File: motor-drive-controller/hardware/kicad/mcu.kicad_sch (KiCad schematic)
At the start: 23 parts, among them J2 Conn_01x03_Pin, J3 JTAG, J4 J_HALL, SW1 SW_Push, U1 STM32F405RGT6, U2 CR2032, Y1 AAH-181-8.000MHZ

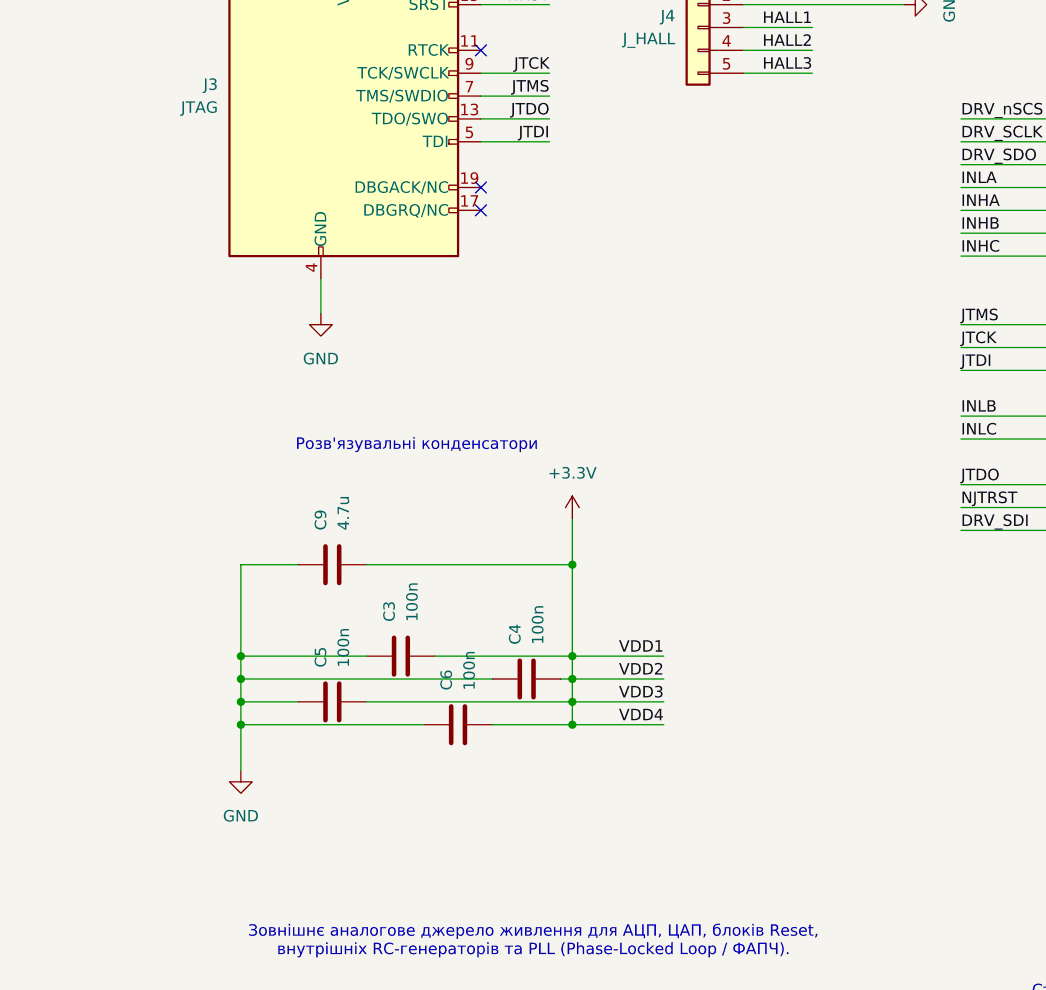
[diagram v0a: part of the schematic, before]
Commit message: feat(motor-drive): add Pull-up resistor to DRV_SDO SPI1
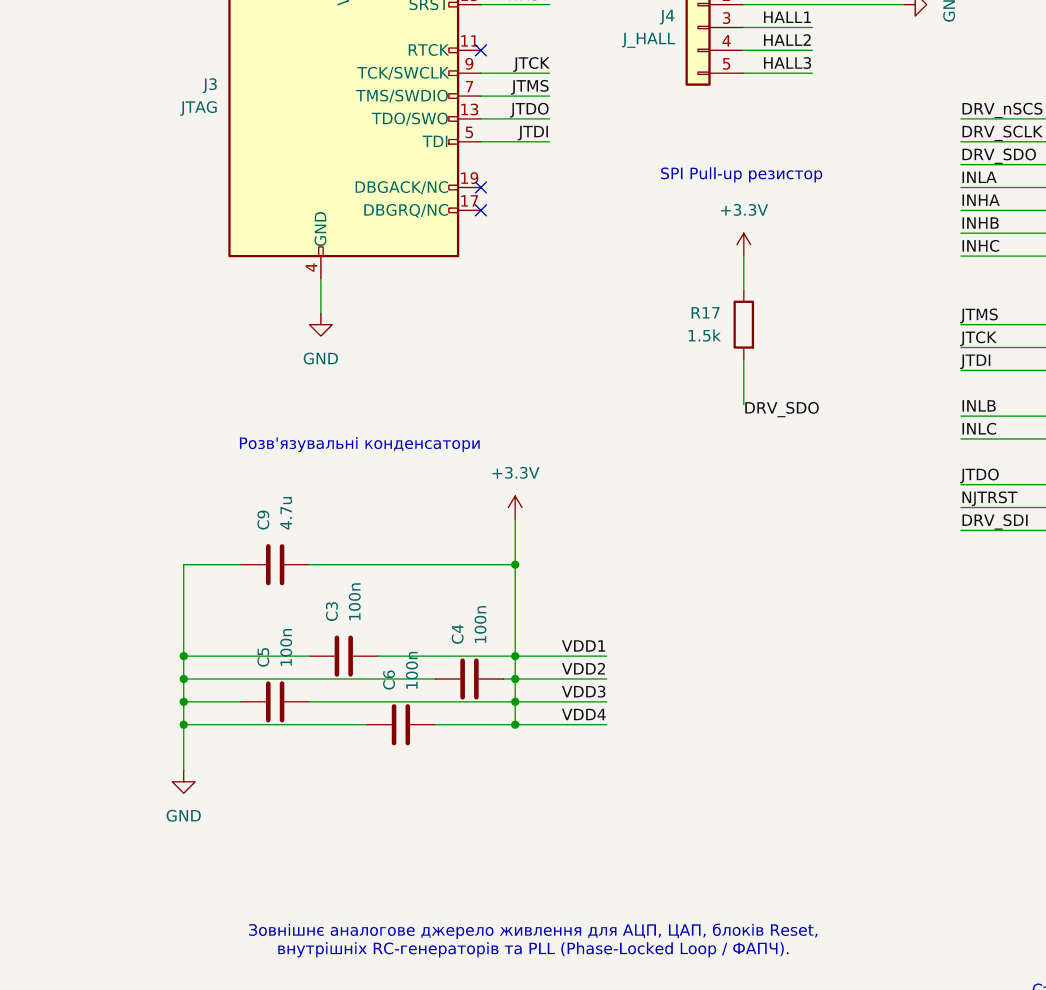
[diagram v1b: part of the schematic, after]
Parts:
- added R17: 1.5k, symbol Device:R
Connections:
- net +3.3V: now also R17.1
- net DRV_SDO: now also R17.2
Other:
- note added: "SPI Pull-up резистор"
- moved on the sheet: C3, C4, C5, C6, C9

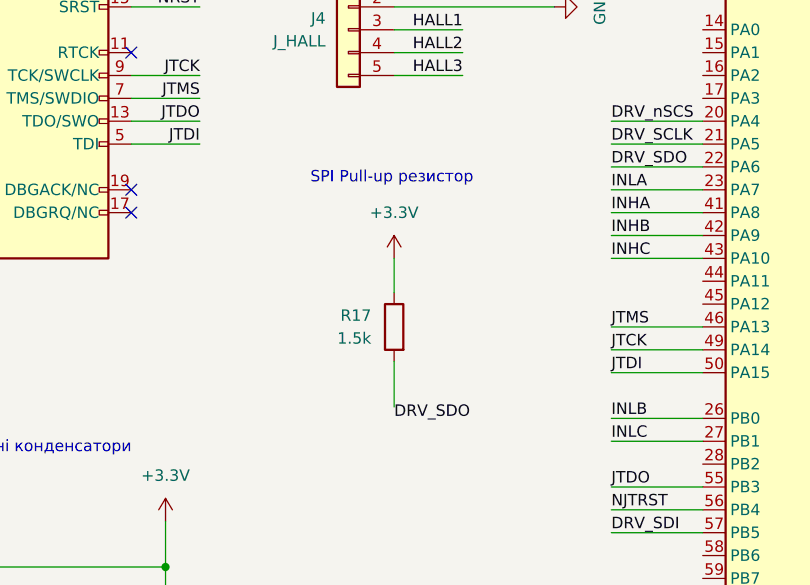
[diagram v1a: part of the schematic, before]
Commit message: feat(motor-drive): add Pull-up resistor to DRV_nSCS SPI1
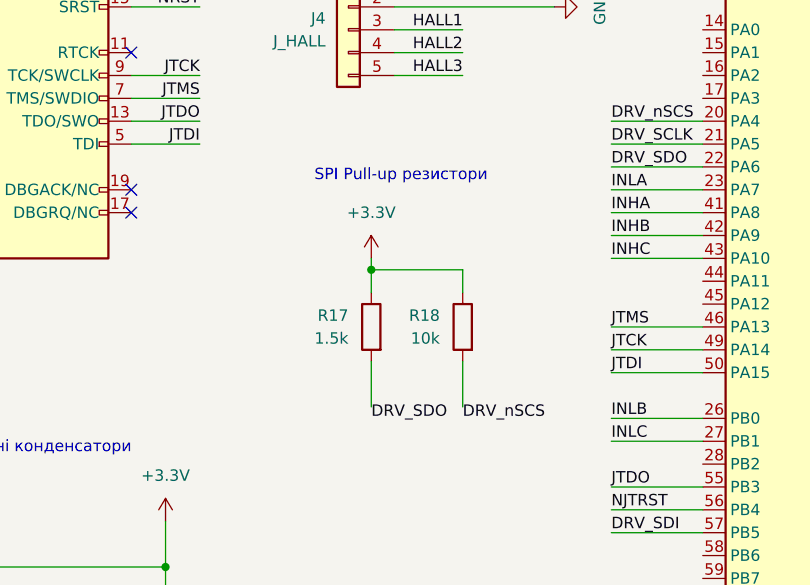
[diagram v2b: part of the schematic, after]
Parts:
- added R18: 10k, symbol Device:R
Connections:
- net +3.3V: now also R18.1
- net DRV_nSCS: now also R18.2
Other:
- note added: "SPI Pull-up резистори"
- note removed: "SPI Pull-up резистор"
- moved on the sheet: R17
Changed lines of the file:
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@@
 		)
 	)
-	(text "SPI Pull-up резистор"
+	(text "SPI Pull-up резистори"
 		(exclude_from_sim no)
-		(at 88.646 64.77 0)
+		(at 89.662 64.516 0)
 		(effects
 			(font
@@
 	)
 	(junction
+		(at 86.36 74.93)
+		(diameter 0)
+		(color 0 0 0 0)
+	)
+	(junction
 		(at 246.38 39.37)
 		(diameter 0)
@@
 	(wire
 		(pts
+			(xy 96.52 74.93) (xy 86.36 74.93)
+		)
+		(stroke
+			(width 0)
+			(type default)
+		)
+	)
+	(wire
+		(pts
 			(xy 238.76 44.45) (xy 240.03 44.45)
 		)
@@
 	(wire
 		(pts
+			(xy 86.36 74.93) (xy 86.36 77.47)
+		)
+		(stroke
+			(width 0)
+			(type default)
+		)
+	)
+	(wire
+		(pts
 			(xy 73.66 123.19) (xy 63.5 123.19)
 		)
@@
 	(wire
 		(pts
-			(xy 88.9 73.66) (xy 88.9 77.47)
+			(xy 86.36 73.66) (xy 86.36 74.93)
 		)
 		(stroke
@@
 	(wire
 		(pts
-			(xy 88.9 90.17) (xy 88.9 85.09)
+			(xy 86.36 90.17) (xy 86.36 85.09)
 		)
 		(stroke
@@
 	(wire
 		(pts
+			(xy 96.52 74.93) (xy 96.52 77.47)
+		)
+		(stroke
+			(width 0)
+			(type default)
+		)
+	)
+	(wire
+		(pts
+			(xy 96.52 85.09) (xy 96.52 90.17)
+		)
+		(stroke
+			(width 0)
+			(type default)
+		)
+	)
+	(wire
+		(pts
 			(xy 95.25 35.56) (xy 95.25 39.37)
 		)
@@
 	)
 	(label "DRV_SDO"
-		(at 88.9 90.17 0)
+		(at 86.36 90.17 0)
+		(effects
+			(font
+				(size 1.27 1.27)
+			)
+			(justify top)
+		)
+	)
+	(label "DRV_nSCS"
+		(at 96.52 90.17 0)
 		(effects
 			(font
@@
 	(symbol
 		(lib_id "power:+3.3V")
-		(at 88.9 73.66 0)
+		(at 86.36 73.66 0)
 		(unit 1)
 		(body_style 1)
@@
 		(fields_autoplaced yes)
 		(property "Reference" "#PWR040"
-			(at 88.9 77.47 0)
+			(at 86.36 77.47 0)
 			(hide yes)
 			(show_name no)
@@
 		)
 		(property "Value" "+3.3V"
-			(at 88.9 68.58 0)
+			(at 86.36 68.58 0)
 			(show_name no)
 			(do_not_autoplace no)
@@
 		)
 		(property "Footprint" ""
-			(at 88.9 73.66 0)
+			(at 86.36 73.66 0)
 			(hide yes)
 			(show_name no)
@@
 		)
 		(property "Datasheet" ""
-			(at 88.9 73.66 0)
+			(at 86.36 73.66 0)
 			(hide yes)
 			(show_name no)
@@
 		)
 		(property "Description" "Power symbol creates a global label with name \"+3.3V\""
-			(at 88.9 73.66 0)
+			(at 86.36 73.66 0)
 			(hide yes)
 			(show_name no)
@@
 	)
 	(symbol
+		(lib_id "Device:R")
+		(at 96.52 81.28 0)
+		(mirror y)
+		(unit 1)
+		(body_style 1)
+		(exclude_from_sim no)
+		(in_bom yes)
+		(on_board yes)
+		(in_pos_files yes)
+		(dnp no)
+		(fields_autoplaced yes)
+		(property "Reference" "R18"
+			(at 93.98 80.0099 0)
+			(show_name no)
+			(do_not_autoplace no)
+			(effects
+				(font
+					(size 1.27 1.27)
+				)
+				(justify left)
+			)
+		)
+		(property "Value" "10k"
+			(at 93.98 82.5499 0)
+			(show_name no)
+			(do_not_autoplace no)
+			(effects
+				(font
+					(size 1.27 1.27)
+				)
+				(justify left)
+			)
+		)
+		(property "Footprint" ""
+			(at 98.298 81.28 90)
+			(hide yes)
+			(show_name no)
+			(do_not_autoplace no)
+			(effects
+				(font
+					(size 1.27 1.27)
+				)
+			)
+		)
+		(property "Datasheet" ""
+			(at 96.52 81.28 0)
+			(hide yes)
+			(show_name no)
+			(do_not_autoplace no)
+			(effects
+				(font
+					(size 1.27 1.27)
+				)
+			)
+		)
+		(property "Description" "Resistor"
+			(at 96.52 81.28 0)
+			(hide yes)
+			(show_name no)
+			(do_not_autoplace no)
+			(effects
+				(font
+					(size 1.27 1.27)
+				)
+			)
+		)
+		(pin "1"
+		)
+		(pin "2"
+		)
+		(instances
+			(project "motor-drive-controller"
+				(path "/b8e0307a-d356-4cd3-91c6-dd251b6e910b/194c8782-4fa9-42ae-9e6d-f27cf422e161"
+					(reference "R18")
+					(unit 1)
+				)
+			)
+		)
+	)
+	(symbol
 		(lib_id "power:+5V")
 		(at 95.25 35.56 0)
@@
 	(symbol
 		(lib_id "Device:R")
-		(at 88.9 81.28 0)
+		(at 86.36 81.28 0)
 		(mirror y)
 		(unit 1)
@@
 		(fields_autoplaced yes)
 		(property "Reference" "R17"
-			(at 86.36 80.0099 0)
+			(at 83.82 80.0099 0)
 			(show_name no)
 			(do_not_autoplace no)
@@
 		)
 		(property "Value" "1.5k"
-			(at 86.36 82.5499 0)
+			(at 83.82 82.5499 0)
 			(show_name no)
 			(do_not_autoplace no)
@@
 		)
 		(property "Footprint" ""
-			(at 90.678 81.28 90)
+			(at 88.138 81.28 90)
 			(hide yes)
 			(show_name no)
@@
 		)
 		(property "Datasheet" ""
-			(at 88.9 81.28 0)
+			(at 86.36 81.28 0)
 			(hide yes)
 			(show_name no)
@@
 		)
 		(property "Description" "Resistor"
-			(at 88.9 81.28 0)
+			(at 86.36 81.28 0)
 			(hide yes)
 			(show_name no)

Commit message: feat(hw09): create links between labels of different hierarchical sheets
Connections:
- net DRV_SDO: no longer U1.22 (PA6)
- net DRV_nSCS: no longer U1.20 (PA4)
- net DRV_PWRGD renamed DRV.PWRGD
- net DRV_SCLK renamed DRV.SCLK
- net DRV_SDI renamed DRV.SDI
- net DRV_nFAULT renamed DRV.nFAULT
- net INHA renamed DRV.INHA
- net INHB renamed DRV.INHB
- net INHC renamed DRV.INHC
- net INLA renamed DRV.INLA
- net INLB renamed DRV.INLB
- net INLC renamed DRV.INLC
- new net DRV.SDO: U1.22 (PA6)
- new net DRV.nSCS: U1.20 (PA4)
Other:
- moved on the sheet: C10, C11, C7, C8, FL1, R17, R18

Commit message: feat(hw09): rename net labels
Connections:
- net DRV_SDO is gone; now on net DRV.SDO: R17.2
- net DRV_nSCS is gone; now on net DRV.nSCS: R18.2
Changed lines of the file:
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@@
 		)
 	)
-	(label "DRV_SDO"
+	(label "DRV.SDO"
 		(at 152.4 181.61 0)
 		(effects
@@
 		)
 	)
-	(label "DRV_nSCS"
+	(label "DRV.nSCS"
 		(at 162.56 181.61 0)
 		(effects

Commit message: feat(hw09): add ISENSE ADC channels and update schematics
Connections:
- net ISENSE.SO2: now reaches U1.10 (PC2)
- net ISENSE.SO3: now reaches U1.11 (PC3)
- net ISENSE.SO1: now reaches U1.9 (PC1)
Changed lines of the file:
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@@
+	)
+	(bus_entry
+		(at 179.07 83.82)
+		(size -2.54 -2.54)
+		(stroke
+			(width 0)
+			(type default)
+		)
 	)
 	(bus_entry
@@
 	)
 	(bus_entry
+		(at 179.07 76.2)
+		(size -2.54 -2.54)
+		(stroke
+			(width 0)
+			(type default)
+		)
+	)
+	(bus_entry
 		(at 110.49 68.58)
 		(size 2.54 -2.54)
-		(stroke
-			(width 0)
-			(type default)
-		)
-	)
-	(bus_entry
-		(at 179.07 81.28)
-		(size -2.54 2.54)
 		(stroke
 			(width 0)
@@
 	)
 	(bus_entry
+		(at 179.07 78.74)
+		(size -2.54 -2.54)
+		(stroke
+			(width 0)
+			(type default)
+		)
+	)
+	(bus_entry
+		(at 179.07 81.28)
+		(size -2.54 -2.54)
+		(stroke
+			(width 0)
+			(type default)
+		)
+	)
+	(bus_entry
 		(at 110.49 93.98)
 		(size 2.54 -2.54)
@@
 	)
 	(bus_entry
-		(at 179.07 78.74)
-		(size -2.54 2.54)
+		(at 179.07 86.36)
+		(size -2.54 -2.54)
 		(stroke
 			(width 0)
@@
 	(bus
 		(pts
-			(xy 179.07 81.28) (xy 179.07 76.2)
+			(xy 179.07 83.82) (xy 179.07 88.9)
 		)
 		(stroke
@@
 	(wire
 		(pts
+			(xy 163.83 76.2) (xy 176.53 76.2)
+		)
+		(stroke
+			(width 0)
+			(type default)
+		)
+	)
+	(wire
+		(pts
 			(xy 212.09 39.37) (xy 212.09 41.91)
 		)
@@
 	(wire
 		(pts
+			(xy 163.83 78.74) (xy 176.53 78.74)
+		)
+		(stroke
+			(width 0)
+			(type default)
+		)
+	)
+	(wire
+		(pts
 			(xy 212.09 74.93) (xy 228.6 74.93)
 		)
@@
 	(bus
 		(pts
-			(xy 179.07 76.2) (xy 184.15 76.2)
+			(xy 179.07 88.9) (xy 184.15 88.9)
 		)
 		(stroke
@@
 	(wire
 		(pts
+			(xy 163.83 73.66) (xy 176.53 73.66)
+		)
+		(stroke
+			(width 0)
+			(type default)
+		)
+	)
+	(wire
+		(pts
 			(xy 104.14 176.53) (xy 104.14 180.34)
 		)
@@
 		)
 	)
+	(bus
+		(pts
+			(xy 184.15 81.28) (xy 179.07 81.28)
+		)
+		(stroke
+			(width 0)
+			(type default)
+		)
+	)
 	(wire
 		(pts
@@
 		(pts
 			(xy 229.87 137.16) (xy 229.87 133.35)
+		)
+		(stroke
+			(width 0)
+			(type default)
+		)
+	)
+	(bus
+		(pts
+			(xy 179.07 76.2) (xy 179.07 81.28)
 		)
 		(stroke
@@
 		)
 	)
+	(label "ISENSE.SO2"
+		(at 176.53 76.2 180)
+		(effects
+			(font
+				(size 1.27 1.27)
+			)
+			(justify right bottom)
+		)
+	)
+	(label "DRV.nFAULT"
+		(at 176.53 81.28 180)
+		(effects
+			(font
+				(size 1.27 1.27)
+			)
+			(justify right bottom)
+		)
+	)
 	(label "VDD2"
 		(at 143.51 35.56 0)
@@
 		)
 	)
+	(label "ISENSE.SO1"
+		(at 176.53 73.66 180)
+		(effects
+			(font
+				(size 1.27 1.27)
+			)
+			(justify right bottom)
+		)
+	)
 	(label "VDD1"
 		(at 73.66 118.11 180)
@@
 		)
 	)
+	(label "ISENSE.SO3"
+		(at 176.53 78.74 180)
+		(effects
+			(font
+				(size 1.27 1.27)
+			)
+			(justify right bottom)
+		)
+	)
 	(label "VDD3"
 		(at 140.97 33.02 0)
@@
 			)
 			(justify left bottom)
-		)
-	)
-	(label "DRV.nFAULT"
-		(at 176.53 81.28 180)
-		(effects
-			(font
-				(size 1.27 1.27)
-			)
-			(justify right bottom)
 		)
 	)
@@
 	(hierarchical_label "DRV{STATUS}"
 		(shape input)
-		(at 184.15 76.2 0)
+		(at 184.15 88.9 0)
 		(effects
 			(font
@@
 		(effects
 			(font
+				(size 1.27 1.27)
+			)
+			(justify left)
+		)
+	)
+	(hierarchical_label "ISENSE{ADC3}"
+		(shape input)
+		(at 184.15 81.28 0)
+		(effects
+			(font

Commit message: feat(hw09): update ADC channel names and schematic references to ANALOG prefix
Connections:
- net ISENSE.SO1 renamed ANALOG.SO1
- net ISENSE.SO2 renamed ANALOG.SO2
- net ISENSE.SO3 renamed ANALOG.SO3
- net TEMP_SENSE renamed ANALOG.TEMP
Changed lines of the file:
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@@
+		)
+	)
+	(bus_entry
+		(at 179.07 73.66)
+		(size -2.54 -2.54)
+		(stroke
+			(width 0)
+			(type default)
 		)
 	)
@@
 	(bus
 		(pts
-			(xy 179.07 76.2) (xy 179.07 81.28)
+			(xy 179.07 73.66) (xy 179.07 81.28)
 		)
 		(stroke
@@
 		)
 	)
-	(label "ISENSE.SO2"
+	(label "ANALOG.SO2"
 		(at 176.53 76.2 180)
 		(effects
@@
 		)
 	)
-	(label "ISENSE.SO1"
+	(label "ANALOG.SO1"
 		(at 176.53 73.66 180)
 		(effects
@@
 		)
 	)
-	(label "ISENSE.SO3"
+	(label "ANALOG.SO3"
 		(at 176.53 78.74 180)
 		(effects
@@
 	(label "VDDA"
 		(at 85.09 162.56 180)
+		(effects
+			(font
+				(size 1.27 1.27)
+			)
+			(justify right bottom)
+		)
+	)
+	(label "ANALOG.TEMP"
+		(at 176.53 71.12 180)
 		(effects
 			(font
@@
 		)
 	)
-	(hierarchical_label "TEMP_SENSE"
-		(shape input)
-		(at 176.53 71.12 0)
-		(effects
-			(font
-				(size 1.27 1.27)
-			)
-			(justify left)
-		)
-	)
-	(hierarchical_label "ISENSE{ADC3}"
+	(hierarchical_label "ANALOG{AIN4}"
 		(shape input)
 		(at 184.15 81.28 0)

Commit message: feat(hw09): update README and schematic files with JTAG connector details and resistor additions
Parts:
- added R13, R14, R19: 10k, symbol Device:R
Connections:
- net GND: now also R13.2, R14.2, R19.2
- net at J3.11 (RTCK): now also R13.1
- net at J3.17 (DBGRQ/NC): now also R14.1
- net at J3.19 (DBGACK/NC): now also R19.1
- no-connect marks 3 -> 0
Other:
- moved on the sheet: J3

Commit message: fix(hw09): fix ERC issues
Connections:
- no-connect marks 0 -> 25
